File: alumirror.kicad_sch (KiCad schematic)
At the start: 77 parts, among them J1 USB_C_Receptacle_USB2.0_16P_2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, J2 USB_C_Receptacle_USB2.0_16P_2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, K00 PG1350, K01 PG1350, K02 PG1350, K03 PG1350, K04 PG1350, K05 PG1350, K10 PG1350, K11 PG1350, K12 PG1350, K13 PG1350, K14 PG1350, K15 PG1350, K20 PG1350, K21 PG1350, K22 PG1350, K23 PG1350, K24 PG1350, K25 PG1350_1½U, K30 PG1350_1½U, K31 PG1350/SKQUCAA010, SW1 BOOT, U1 CH552T, U2 CH552T, U3 USBLC6-2P6, U4 USBLC6-2P6

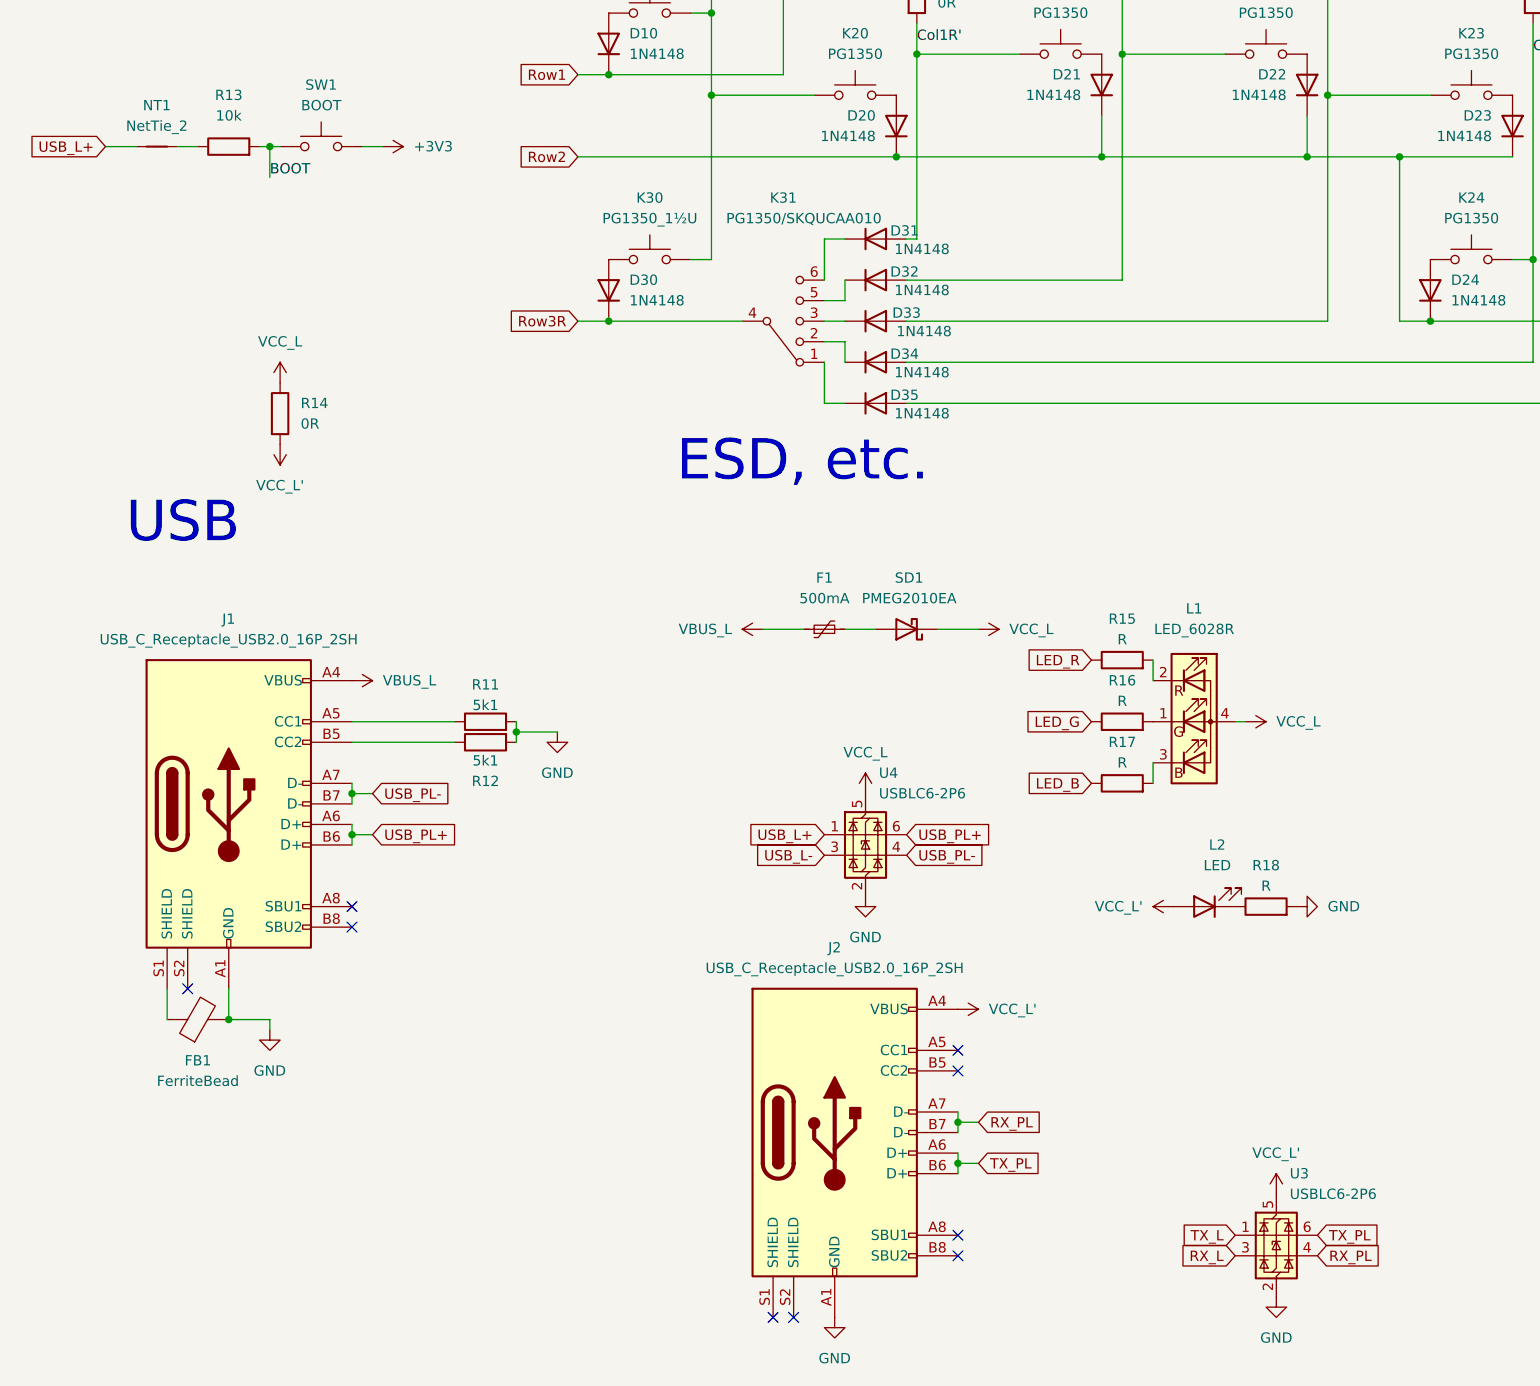
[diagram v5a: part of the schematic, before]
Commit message: Move power LED to middle of PCB above boot switch
Plus various routing tweaks and footprint updates.
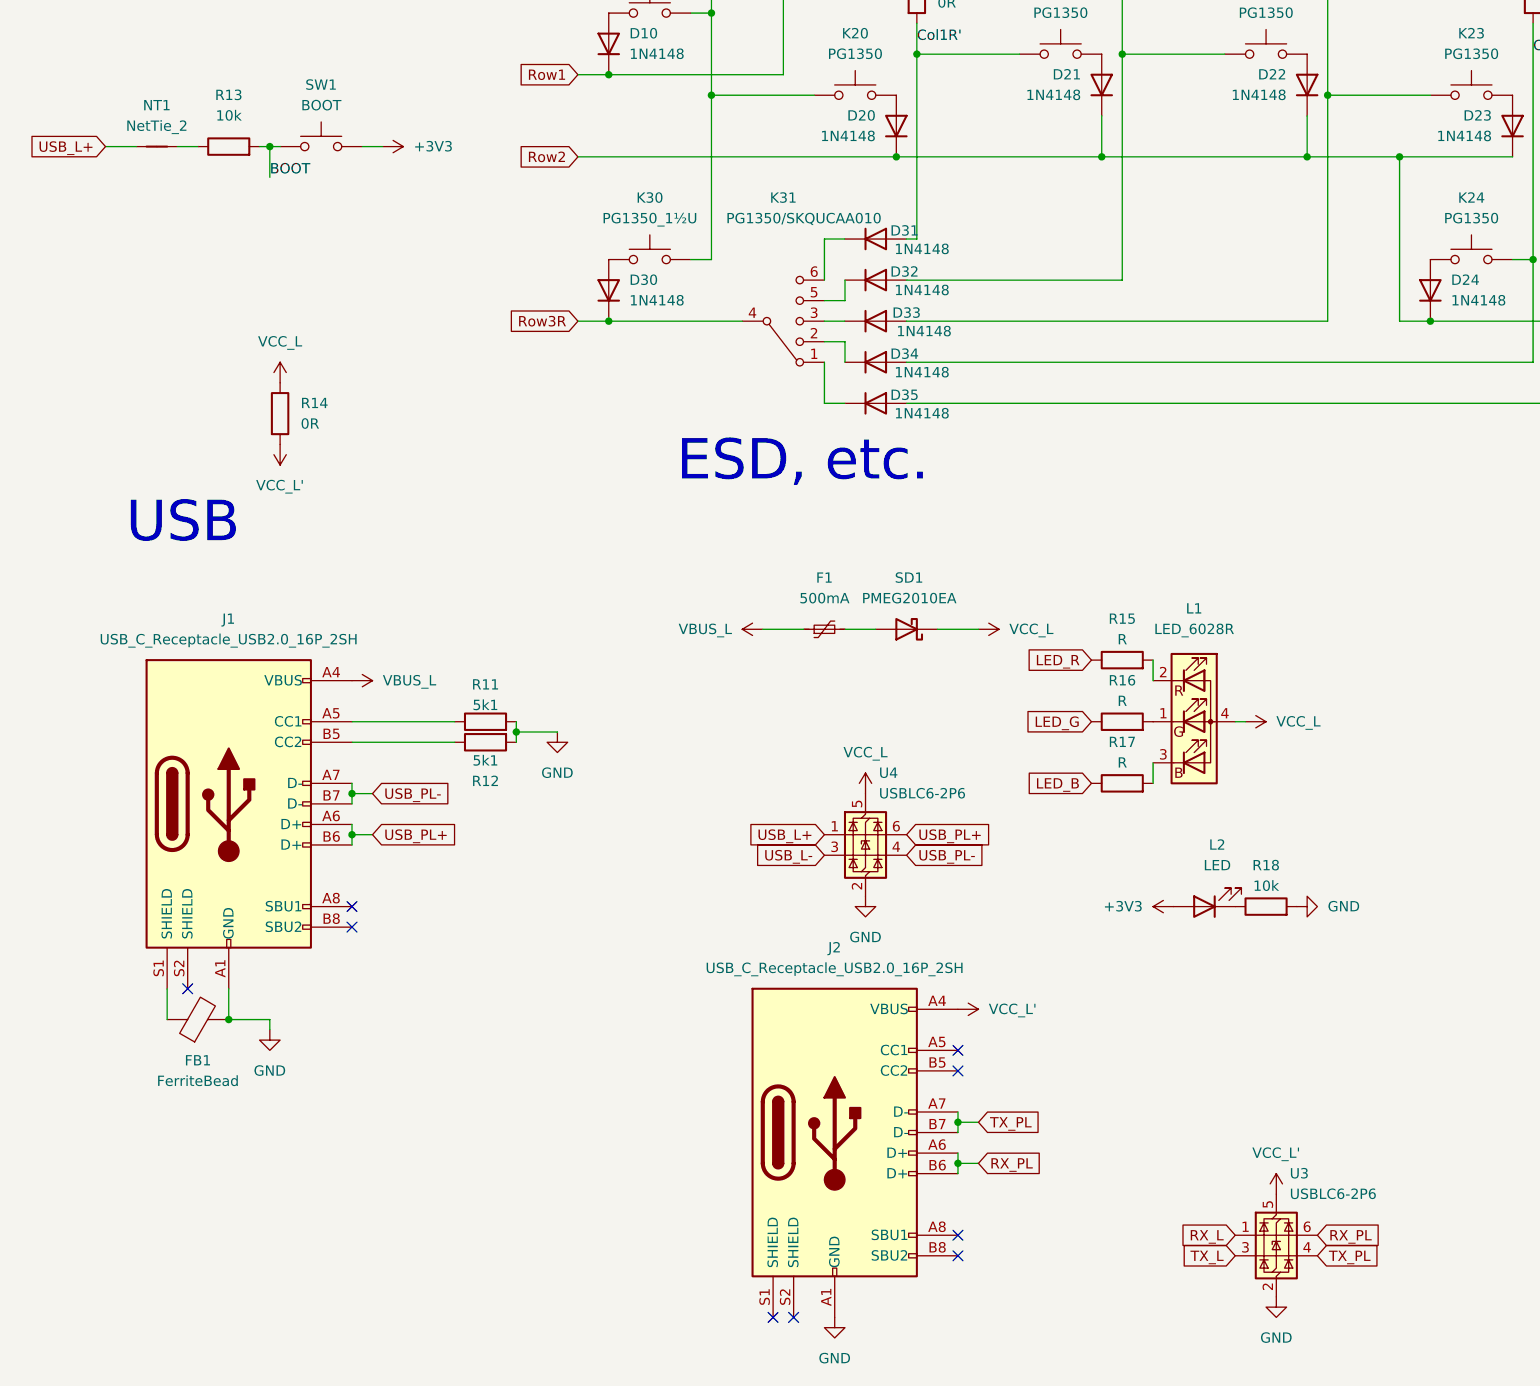
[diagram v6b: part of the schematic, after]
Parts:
- L2: footprint LED_SMD:LED_0603_1608Metric -> Project Library:LED_0603_1608Metric
- R11, R12, R13, R15, R16, R17: footprint Resistor_SMD:R_0603_1608Metric -> Project Library:R_0603_1608Metric_Mod
- R18: value R -> 10k; footprint Resistor_SMD:R_0603_1608Metric -> Project Library:R_0603_1608Metric_Mod
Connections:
- net +3V3: now also L2.2 (A)
- net RX_L: now also U3.1 (I/O1); no longer U3.3 (I/O2)
- net RX_PL: now also J2.A6 (D+), J2.B6 (D+), U3.6 (I/O1); no longer J2.A7 (D-), J2.B7 (D-), U3.4 (I/O2)
- net TX_L: now also U3.3 (I/O2); no longer U3.1 (I/O1)
- net TX_PL: now also J2.A7 (D-), J2.B7 (D-), U3.4 (I/O2); no longer J2.A6 (D+), J2.B6 (D+), U3.6 (I/O1)
- net USB_L+: now also NT1.1; no longer NT1.2
- net VCC_L': no longer L2.2 (A)
- net at R13.1: now also NT1.2; no longer NT1.1
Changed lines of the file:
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@@
 	(global_label "TX_PL"
 		(shape input)
-		(at 167.64 215.9 0)
+		(at 167.64 218.44 0)
 		(fields_autoplaced yes)
 		(effects
@@
 		)
 		(property "Intersheetrefs" "${INTERSHEET_REFS}"
-			(at 176.068 215.9 0)
+			(at 176.068 218.44 0)
 			(effects
 				(font
@@
 	(global_label "RX_PL"
 		(shape input)
-		(at 125.73 201.93 0)
+		(at 125.73 207.01 0)
 		(fields_autoplaced yes)
 		(effects
@@
 		)
 		(property "Intersheetrefs" "${INTERSHEET_REFS}"
-			(at 134.4604 201.93 0)
+			(at 134.4604 207.01 0)
 			(effects
 				(font
@@
 	(global_label "RX_L"
 		(shape input)
-		(at 157.48 218.44 180)
+		(at 157.48 215.9 180)
 		(fields_autoplaced yes)
 		(effects
@@
 		)
 		(property "Intersheetrefs" "${INTERSHEET_REFS}"
-			(at 150.0196 218.44 0)
+			(at 150.0196 215.9 0)
 			(effects
 				(font
@@
 	(global_label "TX_L"
 		(shape input)
-		(at 157.48 215.9 180)
+		(at 157.48 218.44 180)
 		(fields_autoplaced yes)
 		(effects
@@
 		)
 		(property "Intersheetrefs" "${INTERSHEET_REFS}"
-			(at 150.322 215.9 0)
+			(at 150.322 218.44 0)
 			(effects
 				(font
@@
 	(global_label "TX_PL"
 		(shape input)
-		(at 125.73 207.01 0)
+		(at 125.73 201.93 0)
 		(fields_autoplaced yes)
 		(effects
@@
 		)
 		(property "Intersheetrefs" "${INTERSHEET_REFS}"
-			(at 134.158 207.01 0)
+			(at 134.158 201.93 0)
 			(effects
 				(font
@@
 	(global_label "RX_PL"
 		(shape input)
-		(at 167.64 218.44 0)
+		(at 167.64 215.9 0)
 		(fields_autoplaced yes)
 		(effects
@@
 		)
 		(property "Intersheetrefs" "${INTERSHEET_REFS}"
-			(at 176.3704 218.44 0)
+			(at 176.3704 215.9 0)
 			(effects
 				(font
@@
 			)
 		)
-		(property "Footprint" "Resistor_SMD:R_0603_1608Metric"
+		(property "Footprint" "Project Library:R_0603_1608Metric_Mod"
 			(at 143.51 161.798 90)
 			(effects
@@
 			)
 		)
-		(property "Footprint" "LED_SMD:LED_0603_1608Metric"
+		(property "Footprint" "Project Library:LED_0603_1608Metric"
 			(at 153.67 175.26 0)
 			(effects
@@
 			)
 		)
-		(property "Footprint" "Resistor_SMD:R_0603_1608Metric"
+		(property "Footprint" "Project Library:R_0603_1608Metric_Mod"
 			(at 143.51 154.178 90)
 			(effects
@@
 			)
 		)
-		(property "Footprint" "Resistor_SMD:R_0603_1608Metric"
+		(property "Footprint" "Project Library:R_0603_1608Metric_Mod"
 			(at 143.51 146.558 90)
 			(effects
@@
 			)
 		)
-		(property "Footprint" "Resistor_SMD:R_0603_1608Metric"
+		(property "Footprint" "Project Library:R_0603_1608Metric_Mod"
 			(at 64.77 154.178 90)
 			(effects
@@
 			)
 		)
-		(property "Footprint" "Resistor_SMD:R_0603_1608Metric"
+		(property "Footprint" "Project Library:R_0603_1608Metric_Mod"
 			(at 33.02 83.058 90)
 			(effects
@@
 			)
 		)
-		(property "Value" "VCC_L'"
+		(property "Value" "+3V3"
 			(at 146.05 175.2599 90)
 			(effects
@@
 		(lib_id "Device:NetTie_2")
 		(at 24.13 81.28 0)
-		(mirror y)
 		(unit 1)
 		(exclude_from_sim no)
@@
 			)
 		)
-		(property "Value" "R"
+		(property "Value" "10k"
 			(at 161.29 172.72 90)
 			(effects
@@
 			)
 		)
-		(property "Footprint" "Resistor_SMD:R_0603_1608Metric"
+		(property "Footprint" "Project Library:R_0603_1608Metric_Mod"
 			(at 161.29 177.038 90)
 			(effects
@@
 			)
 		)
-		(property "Footprint" "Resistor_SMD:R_0603_1608Metric"
+		(property "Footprint" "Project Library:R_0603_1608Metric_Mod"
 			(at 64.77 153.162 90)
 			(effects
